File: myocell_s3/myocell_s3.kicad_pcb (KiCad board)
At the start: 4 copper layers, 52 x 67.5 mm, 99 parts, among them J1 Conn_01x08, J2 IN3P, J3 IN3N, J4 IN4P, J5 Battery Connector JC2, J6 IN4N, J7 USB_C_Receptacle_USB2.0_16P, J8 RLD, Q3 DMG3404L, SW1 SW_Push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

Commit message: routing
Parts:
- moved C14 3.82 mm to (197.0, 82.8), turned to 0 degrees
- moved R56 3.51 mm to (173.8, 73.0), turned to -90 degrees
- moved R55 1.77 mm to (177.0, 73.0), turned to 90 degrees
- moved C16 1.46 mm to (173.2, 95.2), turned to 180 degrees
- moved C11 0.81 mm to (197.0, 87.8)
- moved C13 0.81 mm to (197.0, 85.2)
- moved C10 0.68 mm to (197.0, 90.2)
- moved C22 0.53 mm to (179.0, 78.2)
- moved C23 0.53 mm to (179.0, 80.5)
- moved R11 0.51 mm to (173.2, 80.0)
- moved C34 0.34 mm to (169.2, 86.5)
- moved C19 0.18 mm to (179.2, 95.8)
- moved C20 0.18 mm to (176.8, 95.8)
- turned D8 to 180 degrees
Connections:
- R32 pad 2: IO5 -> IO1
- U4 pad 39: unconnected-(U4-IO1-Pad39) -> IO1
- U4 pad 5: IO5 -> unconnected-(U4-IO5-Pad5)
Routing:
- net VIN: track 0.00 -> 28.7 mm
- net /power_supply/VUSB/2.1A: track 11.8 -> 37.6 mm
- net IO0: track 0.00 -> 18.1 mm
- net /power_supply/BAT: track 0.00 -> 15.0 mm
- net +3.3VA: track 0.00 -> 11.3 mm
- net +3.3V: track 6.96 -> 15.1 mm
- net Net-(U2-VREFP): track 0.00 -> 6.38 mm
- net Net-(U2-VCAP2): track 0.00 -> 5.34 mm
- net Net-(U2-VCAP1): track 0.00 -> 5.23 mm
- net Net-(U4-IO3): track 0.00 -> 4.76 mm
- net Net-(U2-VCAP4): track 0.00 -> 4.28 mm
- net IO1: track 0.00 -> 3.71 mm
- net Net-(U2-RLDREF): track 0.00 -> 3.69 mm
- net Net-(U2-VCAP3): track 0.00 -> 3.65 mm
- net Net-(U4-IO46): track 0.00 -> 3.65 mm
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
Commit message: tracing ADS1298
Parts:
- added R34: 100k, Resistor_SMD:R_0805_2012Metric_Pad1.20x1.40mm_HandSolder, F.Cu at (155.5, 61.5)
- moved C38 37.9 mm to (164.8, 87.7), turned to 90 degrees
- moved U8 37.0 mm to (168.1, 88.4), turned to 0 degrees
- moved C39 32.6 mm to (168.2, 85.4), turned to 0 degrees
- moved C34 5.51 mm to (169.5, 81.0)
- moved U6 5.25 mm to (169.5, 77.7)
- moved C36 4.87 mm to (169.5, 74.5)
- moved R17 4.01 mm to (177.0, 92.2), turned to 0 degrees
- moved R13 2.93 mm to (173.5, 97.2)
- moved C40 2.56 mm to (163.8, 81.5), turned to -90 degrees
- moved R29 1.42 mm to (168.0, 93.2)
- moved R28 1.17 mm to (168.0, 95.8)
- moved R12 1.09 mm to (177.0, 89.8)
- moved C15 0.84 mm to (177.0, 87.5)
- moved R11 0.71 mm to (173.8, 80.5)
- moved C18 0.59 mm to (177.0, 85.2)
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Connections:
- J7 pad A1: Net-(J7-GND-PadA1) -> GND
- J7 pad A12: Net-(J7-GND-PadA1) -> GND
- J7 pad B1: Net-(J7-GND-PadA1) -> GND
- J7 pad B12: Net-(J7-GND-PadA1) -> GND
- J7 pad S1: unconnected-(J7-SHIELD-PadS1) -> Net-(J7-SHIELD)
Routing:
- net Net-(J7-SHIELD): track 0.00 -> 21.6 mm
- net VIN: track 28.7 -> 11.6 mm
- net /power_supply/BAT: track 15.0 -> 0.00 mm
- net /power_supply/VUSB/2.1A: track 37.6 -> 24.9 mm
- net +3.3VA: track 11.3 -> 3.39 mm
- net Net-(U2-RLDREF): track 3.69 -> 0.00 mm
- net Net-(U2-VCAP3): track 3.65 -> 0.00 mm
- net /cpu_wroom_esp32/bat_mon: track 2.75 -> 0.00 mm
- net +3.3V: track 15.1 -> 12.6 mm
- net EN: track 27.9 -> 28.6 mm
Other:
- board size 52 x 67.5 mm -> 51 x 67.5 mm

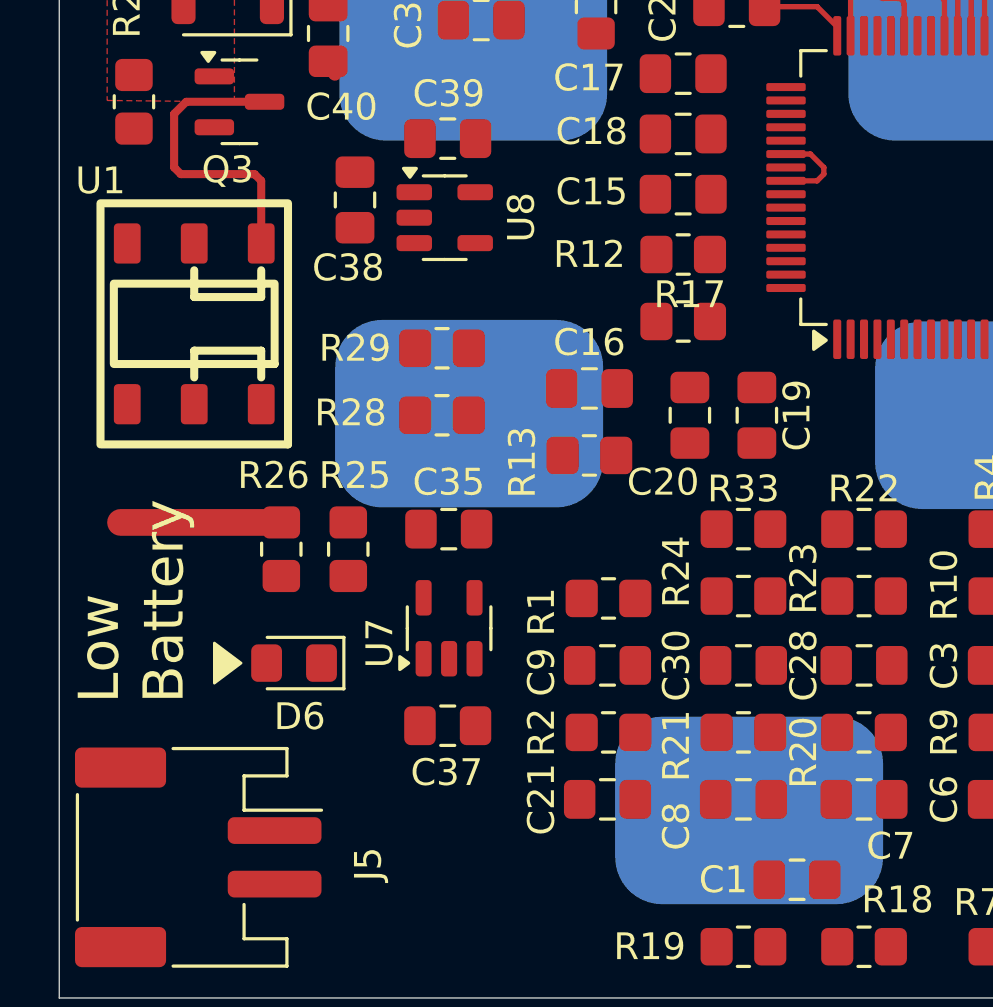
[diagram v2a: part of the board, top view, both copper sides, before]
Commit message: tracing RLD
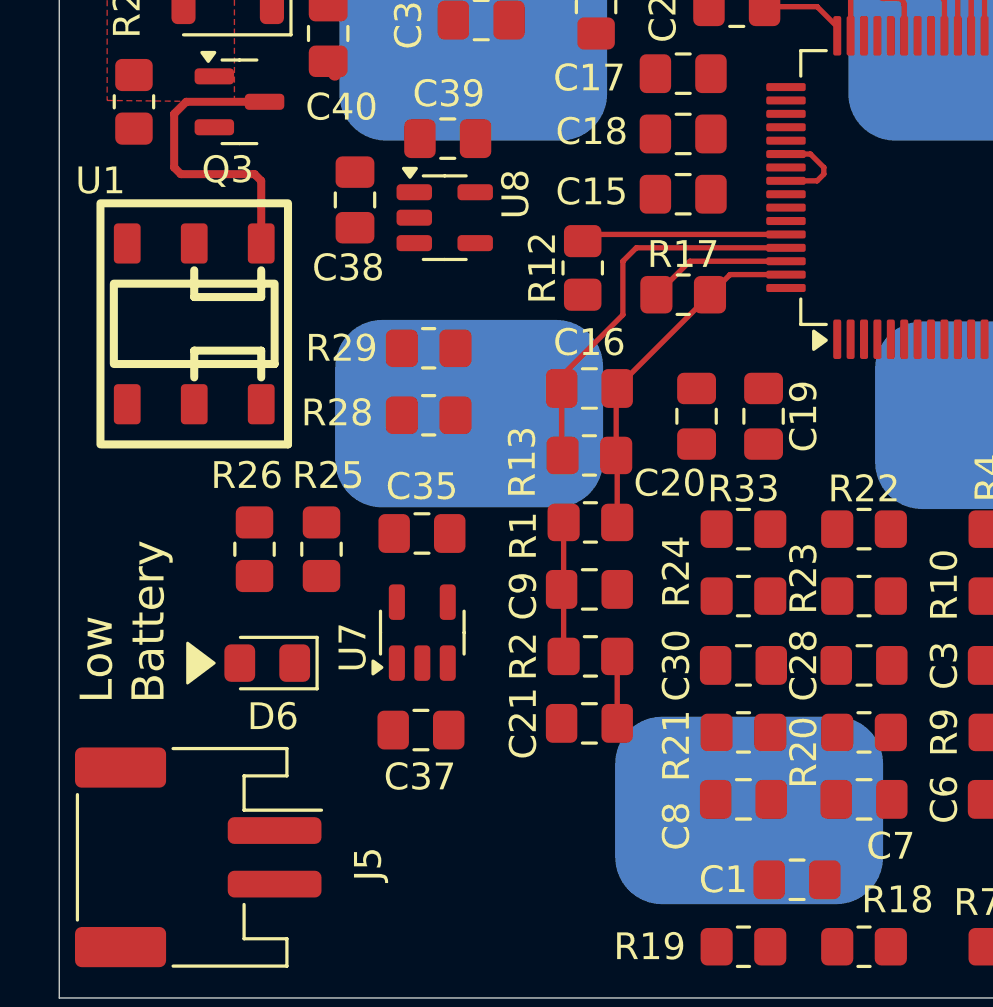
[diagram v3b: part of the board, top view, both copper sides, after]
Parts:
- moved R12 3.78 mm to (173.2, 90.2), turned to 90 degrees
- moved C21 2.92 mm to (173.5, 107.2)
- moved C9 2.92 mm to (173.5, 102.2)
- moved R1 2.92 mm to (173.5, 99.8)
- moved R2 2.92 mm to (173.5, 104.8)
- moved C35 1.01 mm to (167.2, 100.2)
- moved C37 1.01 mm to (167.2, 107.5)
- moved U7 1.01 mm to (167.3, 103.9)
- moved D6 1.00 mm to (161.5, 105.0)
- moved R17 1.00 mm to (177.0, 91.2), turned to 180 degrees
- moved R25 1.00 mm to (163.5, 100.8)
- moved R26 1.00 mm to (161.0, 100.8)
- moved R28 0.50 mm to (167.5, 95.8)
- moved R29 0.50 mm to (167.5, 93.2)
- moved C19 0.25 mm to (180.0, 95.8)
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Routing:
- net RLDINV: track 0.00 -> 14.5 mm
- net Net-(U2-RLDOUT): track 0.00 -> 13.1 mm
- net Net-(U2-RLDREF): track 0.00 -> 7.69 mm
- net /power_supply/VUSB/2.1A: track 24.9 -> 18.9 mm
- net Net-(U2-RLDIN): track 0.00 -> 5.36 mm
- net Net-(C9-Pad2): track 0.00 -> 5.06 mm
- net /adc_8/RLD: track 0.00 -> 2.50 mm

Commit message: tracing pwr
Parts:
- added G***: LOGO, Logo:mirea-2026, F.Cu at (197.0, 71.8)
- moved C36 3.25 mm to (170.7, 77.5), turned to 0 degrees
- moved U6 3.15 mm to (170.9, 80.5), turned to 0 degrees
- moved R11 2.50 mm to (175.2, 78.5)
- moved C34 1.98 mm to (167.5, 80.7), turned to 90 degrees
- moved C38 1.10 mm to (164.8, 88.8)
- moved U8 0.93 mm to (168.1, 89.3)
- moved C39 0.68 mm to (168.2, 86.1)
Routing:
- net +3.3VA: track 3.39 -> 59.5 mm, vias 0 -> 7
- net +3.3V: track 12.6 -> 26.3 mm, vias 0 -> 5
- net VIN: track 11.6 -> 17.8 mm
- added copper zone on In2.Cu, net +3.3V
- added copper zone on In2.Cu, net +3.3VA

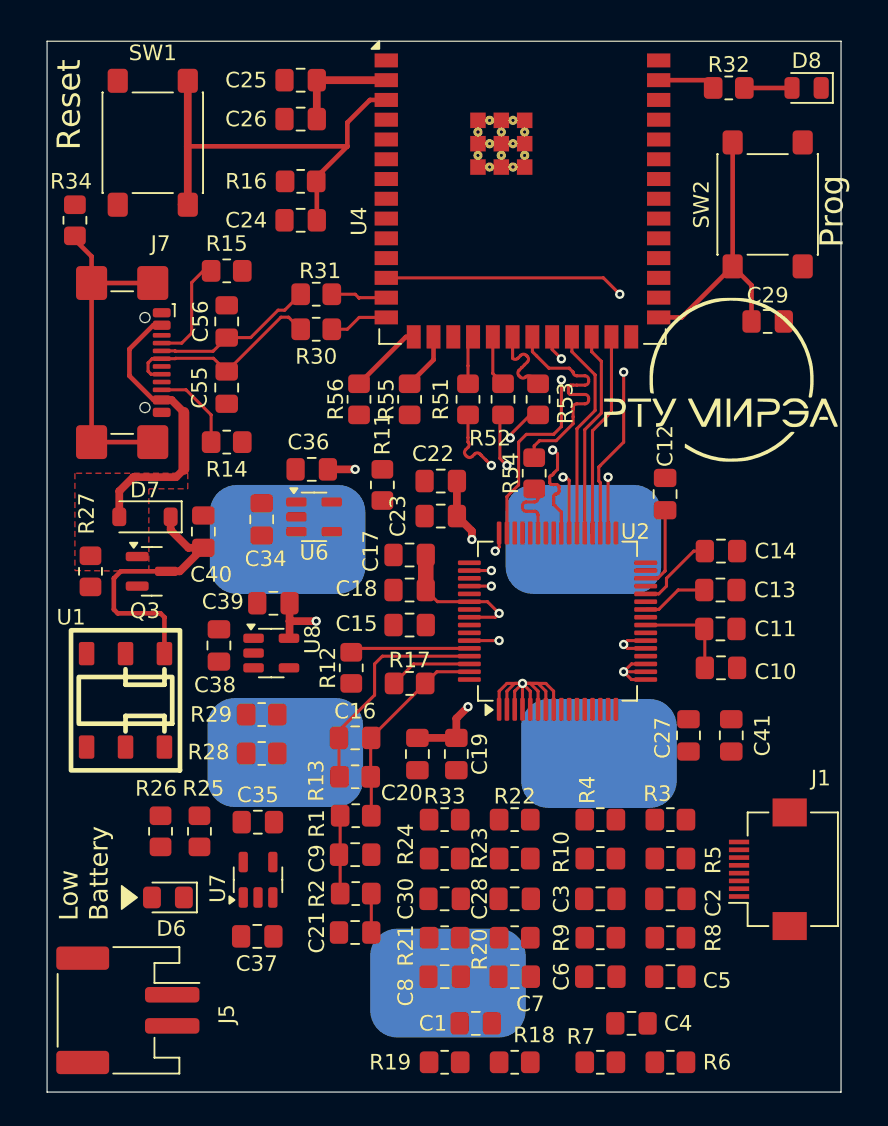
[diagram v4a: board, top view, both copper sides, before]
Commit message: tracing power
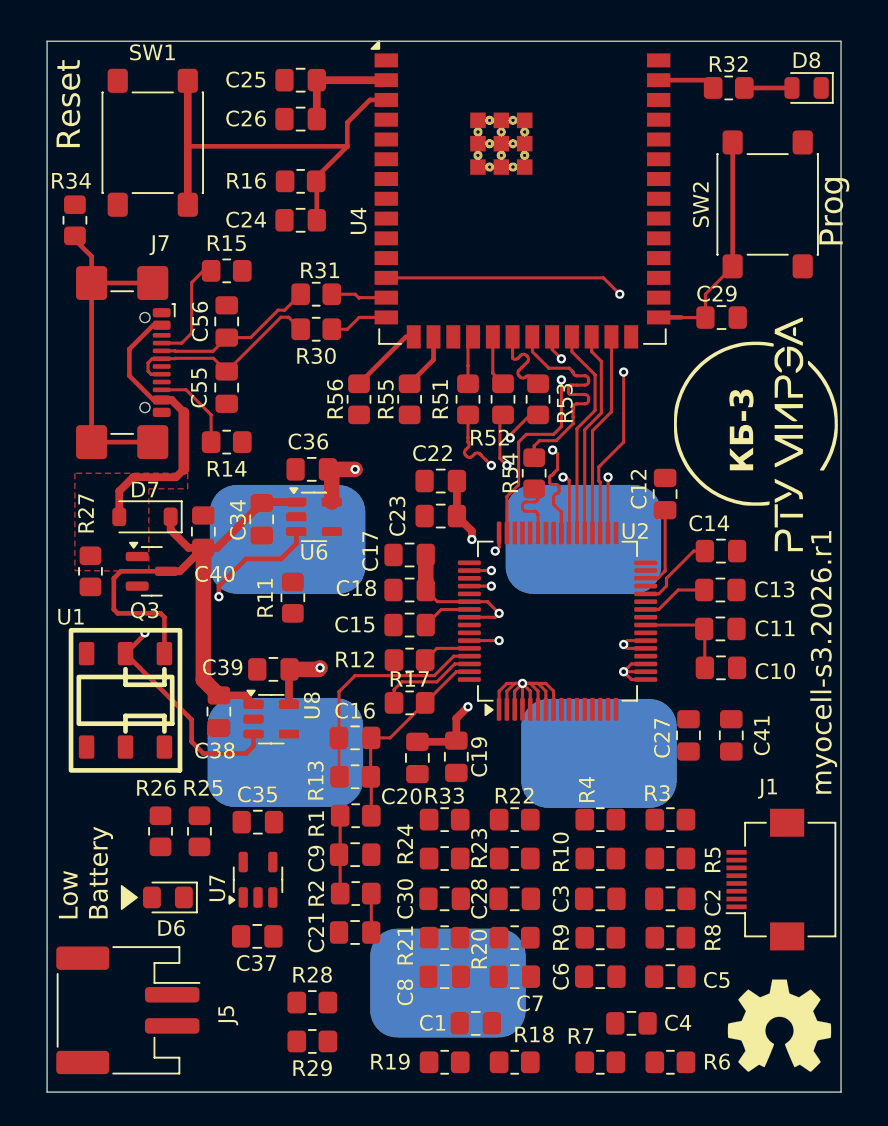
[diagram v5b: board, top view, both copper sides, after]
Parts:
- added REF**: OSHW-Symbol_6.7x6mm_SilkScreen, Symbol:OSHW-Symbol_6.7x6mm_SilkScreen, F.Cu at (200.8, 113.2)
- moved R29 21.2 mm to (170.8, 114.2)
- moved R28 16.3 mm to (170.8, 111.8)
- moved R11 9.25 mm to (169.5, 85.8)
- moved C38 4.25 mm to (164.8, 93.1)
- moved C39 4.25 mm to (168.2, 90.3)
- moved U8 4.25 mm to (168.1, 93.5)
- moved G*** 4.16 mm to (199.2, 75.2), turned to 90 degrees
- moved R12 3.78 mm to (177.0, 89.8), turned to 0 degrees
- moved C29 2.97 mm to (197.0, 67.8)
- moved R17 1.25 mm to (177.0, 92.5)
- moved J1 0.68 mm to (199.8, 103.8)
- moved C20 0.25 mm to (177.5, 96.0)
- moved C19 0.18 mm to (180.0, 96.0)
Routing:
- net PWR_ENA: track 0.00 -> 27.8 mm, vias 0 -> 2
- net VIN: track 17.8 -> 37.3 mm
- net Net-(U2-RLDREF): track 7.69 -> 3.15 mm
- net Net-(U2-VCAP3): track 0.00 -> 3.21 mm
- net IO0: track 18.1 -> 15.0 mm
- net +3.3V: track 26.3 -> 28.5 mm
- net Net-(U2-RLDIN): track 5.36 -> 6.37 mm
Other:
- board text added: "myocell-s3.2026.r1"
- board text added: "КБ-3"

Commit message: tracing analogue interfaces
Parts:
- moved J1 2.51 mm to (199.6, 101.3)
- moved C2 1.01 mm to (192.8, 105.2)
- moved C3 1.01 mm to (188.2, 105.2)
- moved C4 1.01 mm to (190.2, 113.2)
- moved C5 1.01 mm to (192.8, 110.2)
- moved C6 1.01 mm to (188.2, 110.2)
- moved R10 1.01 mm to (188.2, 102.7)
- moved R3 1.01 mm to (192.8, 100.2)
- moved R4 1.01 mm to (188.2, 100.2)
- moved R5 1.01 mm to (192.8, 102.7)
- moved R6 1.01 mm to (192.8, 115.8)
- moved R7 1.01 mm to (188.2, 115.8)
- moved R8 1.01 mm to (192.8, 107.8)
- moved R9 1.01 mm to (188.2, 107.8)
- moved C27 0.88 mm to (195.0, 93.7)
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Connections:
- net /adc_8/IN1N renamed /adc_8/in1-
- net /adc_8/IN1P renamed /adc_8/in1+
- net /adc_8/IN2N renamed /adc_8/in2-
- net /adc_8/IN2P renamed /adc_8/in2+
- net Net-(U2-IN3N) renamed /adc_8/in3-
- net Net-(U2-IN3P) renamed /adc_8/in3+
- net Net-(U2-IN4N) renamed /adc_8/in4-
- net Net-(U2-IN4P) renamed /adc_8/in4+
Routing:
- net /power_supply/BAT: track 0.00 -> 48.8 mm, vias 0 -> 2
- net /power_supply/VUSB/2.1A: track 18.9 -> 55.6 mm, vias 0 -> 2
- net /adc_8/in2-: track 0.00 -> 15.1 mm
- net /adc_8/in2+: track 0.00 -> 14.3 mm
- net /adc_8/in1-: track 0.00 -> 12.7 mm
- net /adc_8/in1+: track 0.00 -> 12.0 mm
- net /adc_8/in4-: track 0.00 -> 11.2 mm
- net /adc_8/in4+: track 0.00 -> 11.2 mm
- net /adc_8/in3-: track 0.00 -> 8.92 mm
- net /adc_8/in3+: track 0.00 -> 8.92 mm
- net +3.3VA: track 60.0 -> 66.4 mm
- net Net-(D6-K): track 0.00 -> 3.81 mm
- net Net-(D6-A): track 0.00 -> 3.48 mm
- net Net-(U7-PROG): track 0.00 -> 3.24 mm
- net /cpu_wroom_esp32/bat_mon: track 0.00 -> 2.50 mm
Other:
- board text added: "myocell-s3.26.r1"
- board text removed: "myocell-s3.2026.r1"

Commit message: tracing analogue interfaces
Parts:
- moved J2 28.7 mm to (193.8, 96.8)
- moved J3 27.9 mm to (193.8, 82.8)
- moved J6 19.5 mm to (169.8, 97.0)
- moved J4 18.4 mm to (169.8, 83.0)
- moved R18 7.25 mm to (176.0, 116.0), turned to 0 degrees
- moved R19 3.72 mm to (176.0, 113.2)
- moved D8 0.69 mm to (201.8, 53.0)
- moved J5 0.25 mm to (158.7, 112.2)
- moved R32 0.25 mm to (197.2, 53.0)
- moved SW1 0.25 mm to (160.5, 56.8)
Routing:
- net +3.3V: track 28.5 -> 62.3 mm, vias 5 -> 7
- net /power_supply/BAT: track 48.8 -> 21.2 mm
- net +3.3VA: track 66.4 -> 76.3 mm, vias 7 -> 11
- net Net-(C1-Pad1): track 0.00 -> 5.69 mm
- net Net-(C1-Pad2): track 0.00 -> 5.55 mm
- net /adc_8/IN4PF: track 0.00 -> 5.10 mm, vias 0 -> 1
- net /adc_8/in4+: track 11.2 -> 16.3 mm
- net /adc_8/in4-: track 11.2 -> 16.3 mm
- net Net-(C30-Pad1): track 0.00 -> 2.52 mm
- net PWR_ENA: track 27.8 -> 28.9 mm
- added copper zone on In2.Cu, net /power_supply/BAT
- added copper zone on In2.Cu, net /power_supply/VUSB/2.1A

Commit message: tracing polygons
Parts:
- moved J8 2.30 mm to (181.8, 110.8)
- moved R7 2.26 mm to (190.5, 116.0), turned to 180 degrees
- moved R6 2.12 mm to (194.2, 114.2), turned to 90 degrees
- moved J5 1.16 mm to (159.2, 111.2)
- moved J4 0.79 mm to (170.5, 82.8)
- moved J6 0.79 mm to (170.5, 96.8)
- moved J2 0.75 mm to (193.0, 96.8)
- moved J3 0.75 mm to (193.0, 82.8)
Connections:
- net /adc_8/IN3NF renamed /adc_8/in3f-
- net /adc_8/IN3PF renamed /adc_8/in3f+
- net /adc_8/IN4NF renamed /adc_8/in4f-
- net /adc_8/IN4PF renamed /adc_8/in4f+
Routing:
- net /adc_8/in3f-: track 0.00 -> 50.0 mm, vias 0 -> 2
- net /adc_8/in3f+: track 0.00 -> 31.8 mm, vias 0 -> 2
- net /adc_8/in4f+: track 5.10 -> 35.4 mm, vias 1 -> 2
- net /adc_8/in4f-: track 0.00 -> 28.9 mm, vias 0 -> 2
- net Net-(C4-Pad1): track 0.00 -> 8.65 mm
- net Net-(C4-Pad2): track 0.00 -> 8.42 mm
- net /adc_8/in3-: track 8.92 -> 14.0 mm
- net /adc_8/in3+: track 8.92 -> 14.0 mm
- net Net-(C3-Pad1): track 0.00 -> 2.52 mm
- net /power_supply/BAT: track 21.2 -> 20.2 mm
- added copper zone on F.Cu, net GNDA
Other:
- board size 51 x 67.5 mm -> 51 x 68 mm
